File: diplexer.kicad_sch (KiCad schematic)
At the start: 5 parts, among them J22 BWSMA-KWE-Z001

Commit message: Start working on BOM, fix supply indoctors
Signed-off-by: Corey Minyard <corey@minyard.net>
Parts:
- L35: footprint Inductor_SMD:L_1206_3216Metric -> Inductor_SMD:L_0805_2012Metric_Pad1.05x1.20mm_HandSolder
- L44: footprint Inductor_SMD:L_1206_3216Metric -> Inductor_SMD:L_0603_1608Metric_Pad1.05x0.95mm_HandSolder
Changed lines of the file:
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@@
 			)
 		)
-		(property "Footprint" "Inductor_SMD:L_1206_3216Metric"
+		(property "Footprint" "Inductor_SMD:L_0603_1608Metric_Pad1.05x0.95mm_HandSolder"
 			(at 102.87 81.28 0)
 			(effects
@@
 			)
 		)
-		(property "Footprint" "Inductor_SMD:L_1206_3216Metric"
+		(property "Footprint" "Inductor_SMD:L_0805_2012Metric_Pad1.05x1.20mm_HandSolder"
 			(at 102.87 105.41 0)
 			(effects

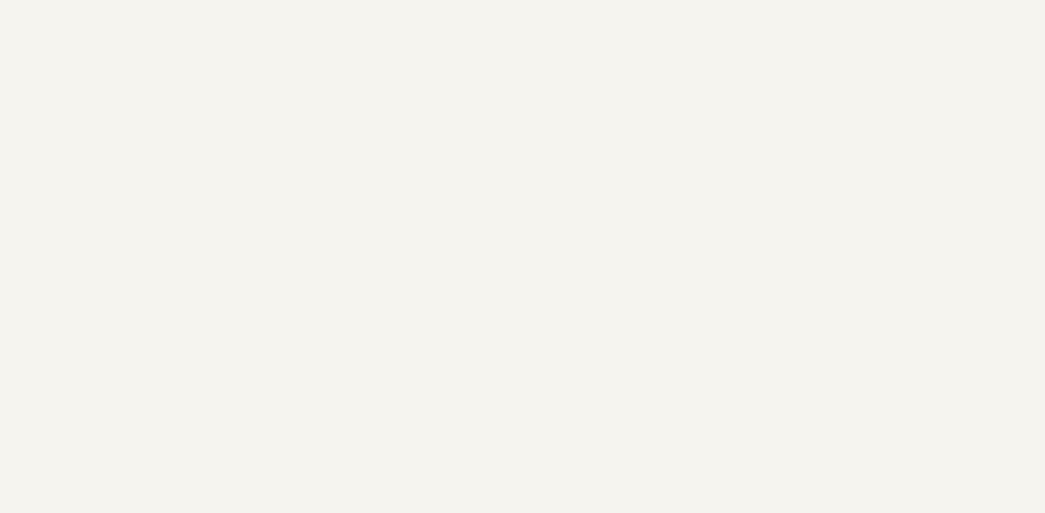
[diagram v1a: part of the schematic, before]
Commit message: Add fiduciaries and a control output
Signed-off-by: Corey Minyard <corey@minyard.net>
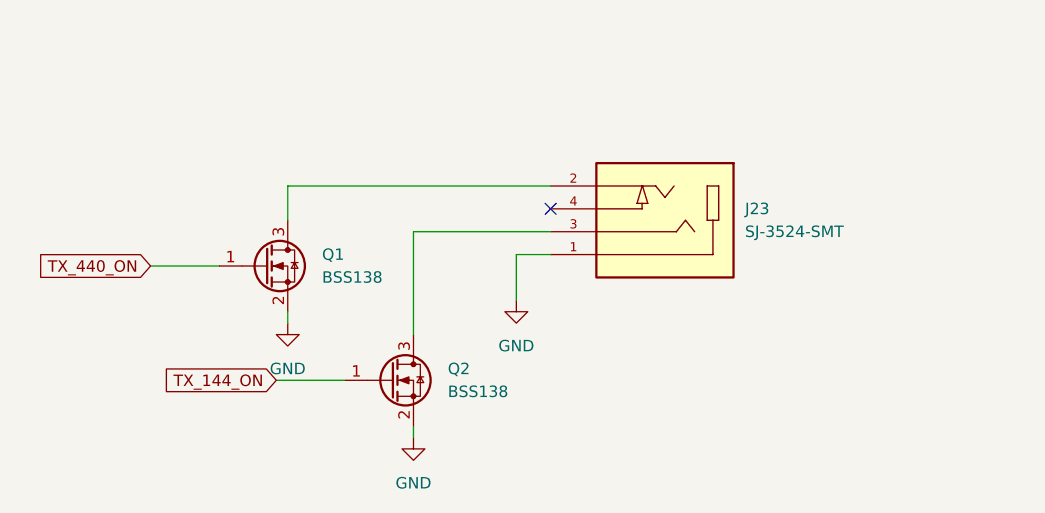
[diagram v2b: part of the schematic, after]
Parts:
- added J23: SJ-3524-SMT, footprints:CUI_SJ-3524-SMT, symbol Local Connectors:SJ-3524-SMT
- added Q1, Q2: BSS138, Package_TO_SOT_SMD:SOT-23, symbol Transistor_FET:BSS138
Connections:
- net GND: now also J23.1, Q1.2 (S), Q2.2 (S)
- new net: J23.2, Q1.3 (D)
- new net: J23.3, Q2.3 (D)
- new net TX_144_ON: Q2.1 (G)
- new net TX_440_ON: Q1.1 (G)
- no-connect marks 0 -> 1

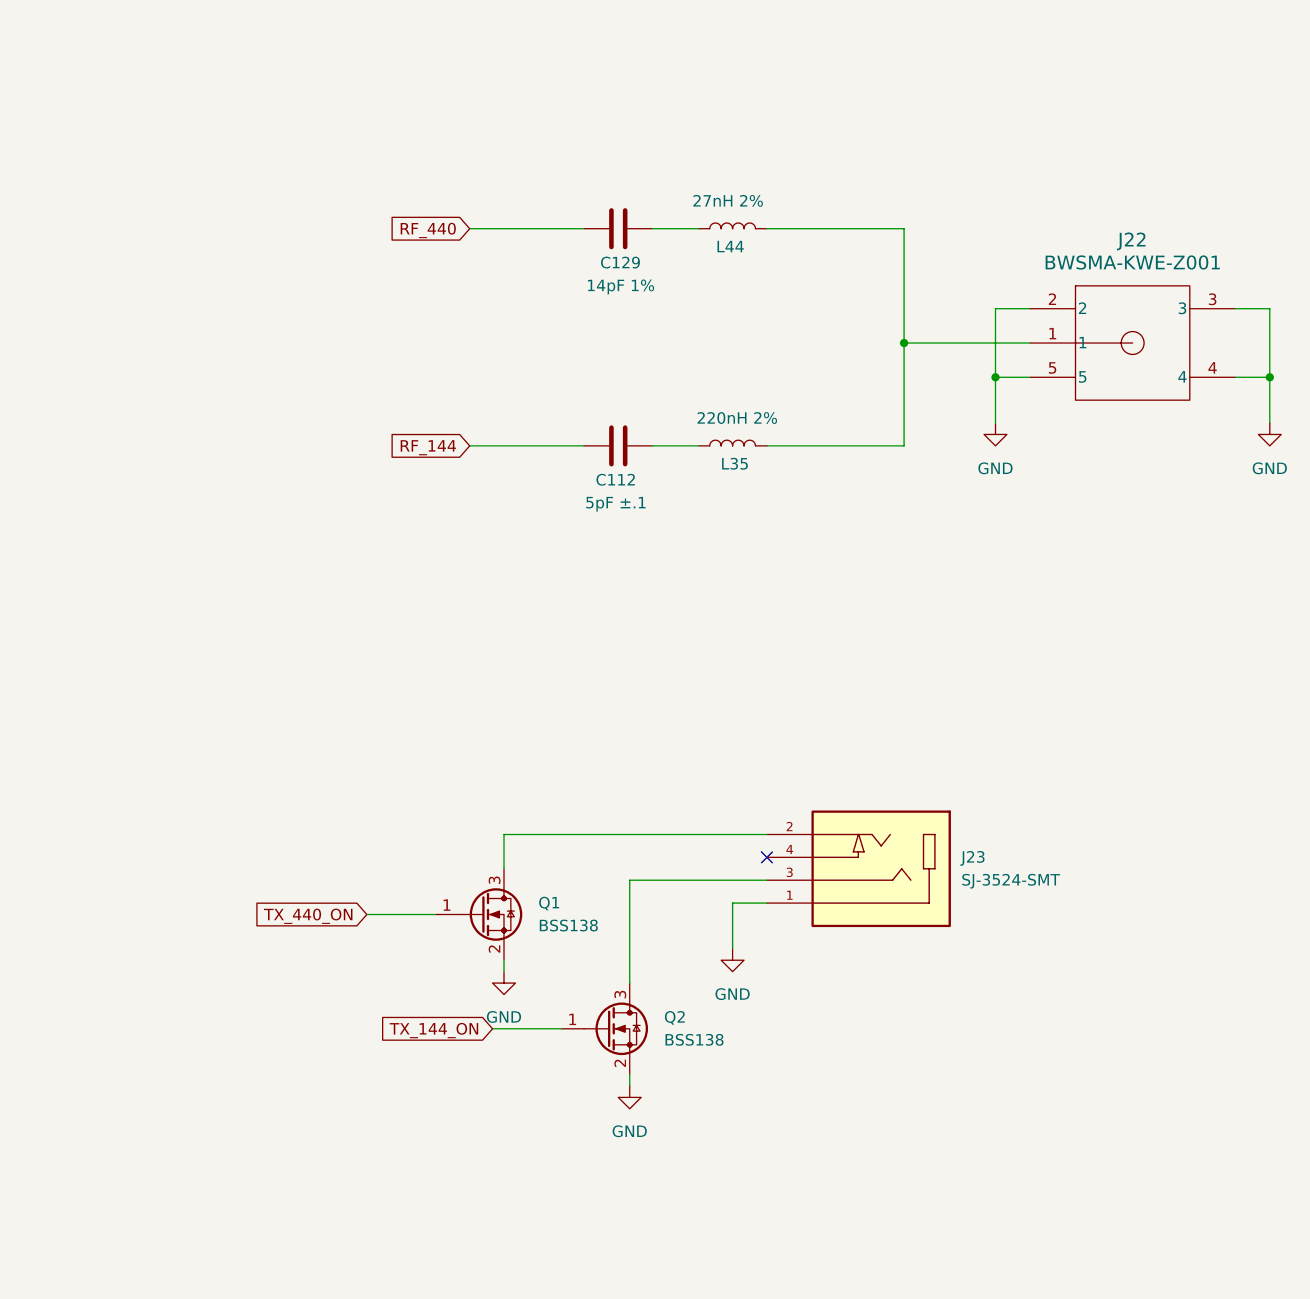
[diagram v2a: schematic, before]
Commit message: Add pull up on the PA enables
So they are off by default.

Signed-off-by: Corey Minyard <corey@minyard.net>
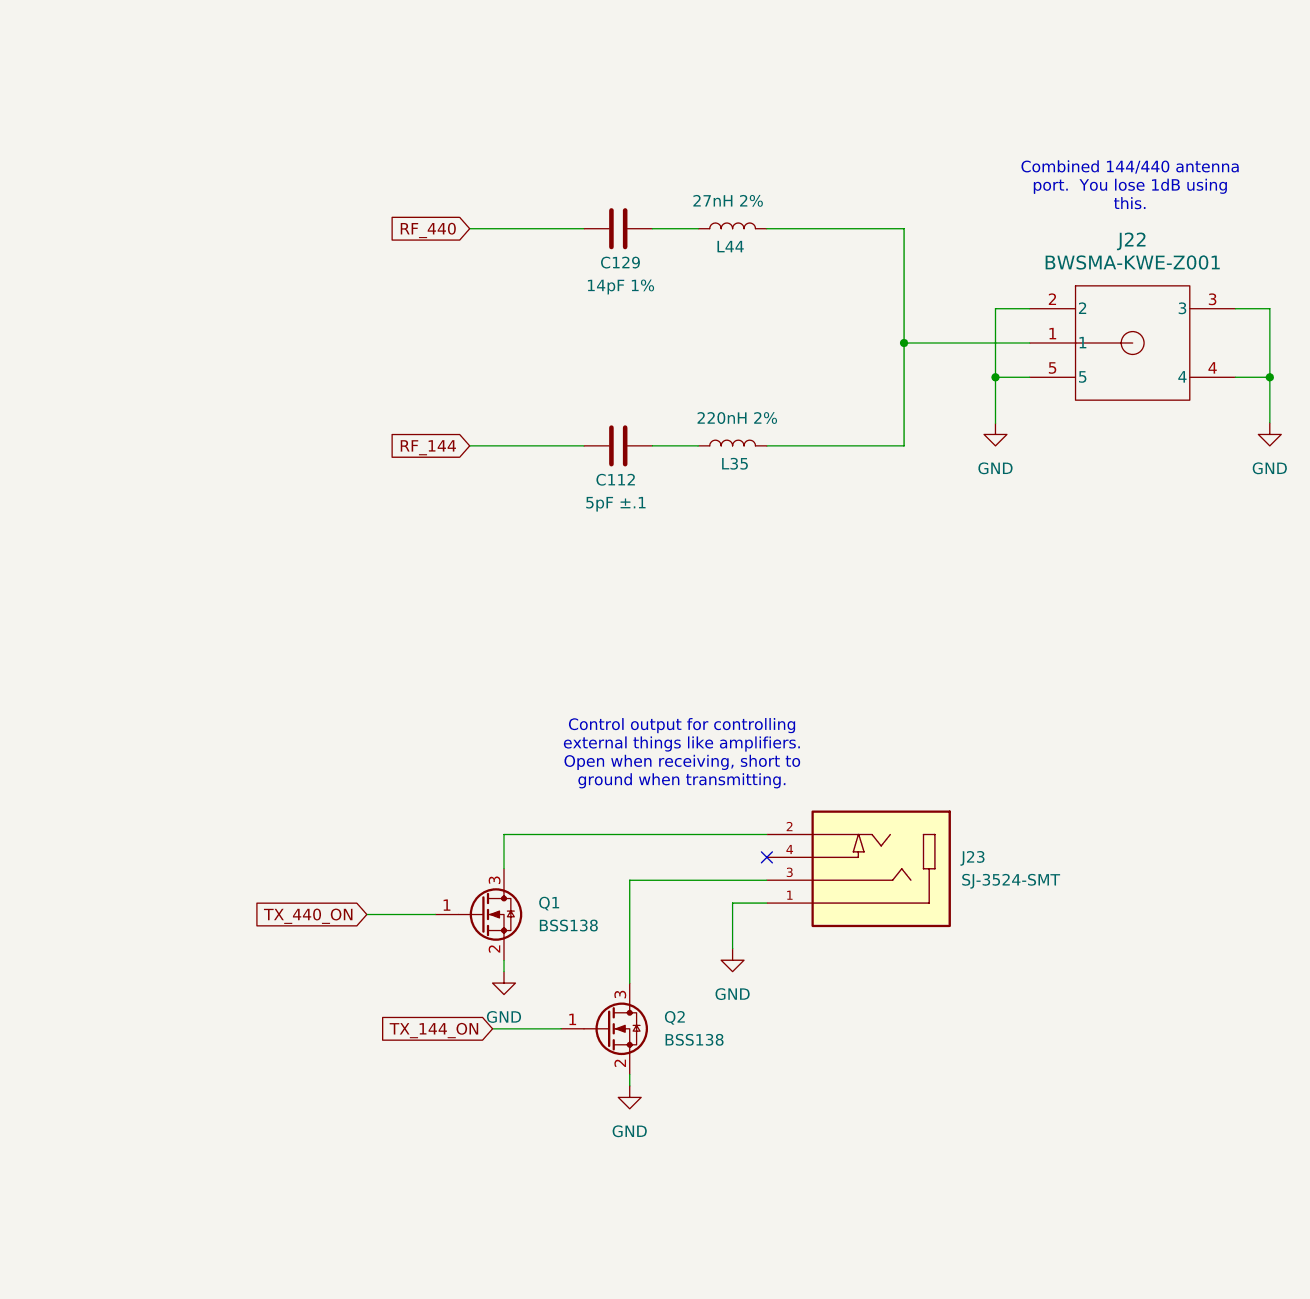
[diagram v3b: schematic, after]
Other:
- note added: "Combined 144/440 antenna port. You lose 1dB using this."
- note added: "Control output for controlling external things like amplifiers. Open when receiving, short to ground when transmitting."
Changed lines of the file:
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@@
 	(generator_version "9.0")
 	(paper "A4")
+	(text "Combined 144/440 antenna\nport.  You lose 1dB using\nthis."
+		(exclude_from_sim no)
+		(at 147.066 76.708 0)
+		(effects
+			(font
+				(size 1.27 1.27)
+			)
+		)
+	)
+	(text "Control output for controlling\nexternal things like amplifiers.\nOpen when receiving, short to\nground when transmitting."
+		(exclude_from_sim no)
+		(at 97.282 139.7 0)
+		(effects
+			(font
+				(size 1.27 1.27)
+			)
+		)
+	)
 	(junction
 		(at 121.92 93.98)

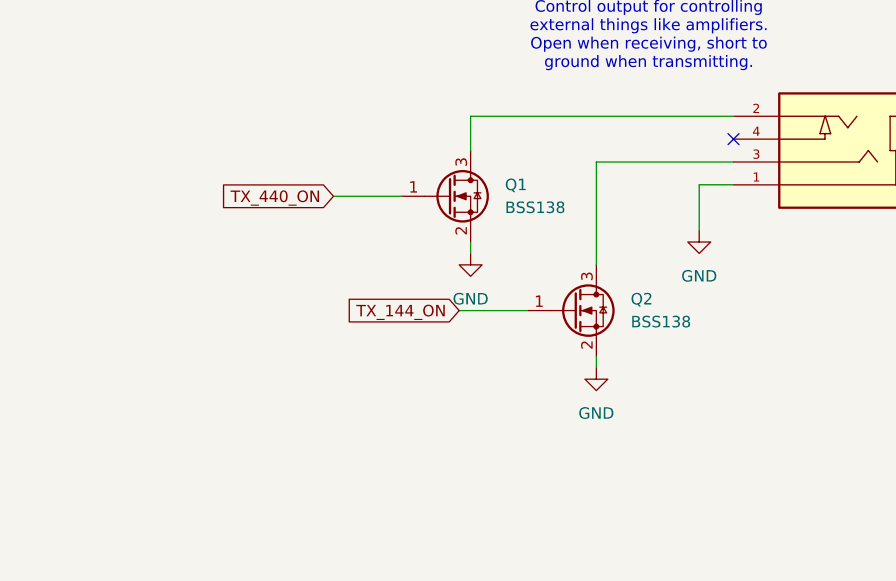
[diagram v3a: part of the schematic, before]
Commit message: Add pulldowns on the external control transistor inputs
So they are disabled by default.

Signed-off-by: Corey Minyard <corey@minyard.net>
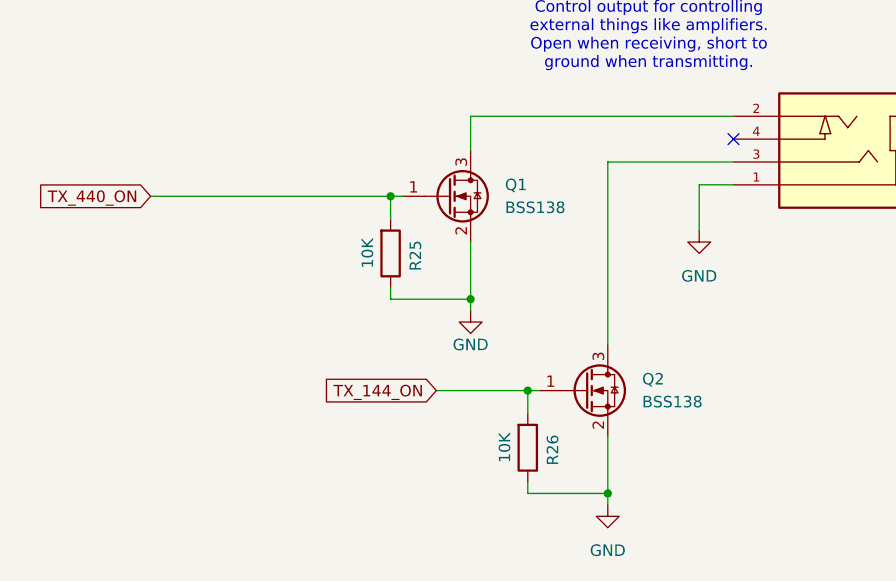
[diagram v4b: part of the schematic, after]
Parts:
- added R25, R26: 10K, Resistor_SMD:R_0402_1005Metric, symbol Device:R
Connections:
- net GND: now also R25.1, R26.1
- net TX_144_ON: now also R26.2
- net TX_440_ON: now also R25.2
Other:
- moved on the sheet: Q2

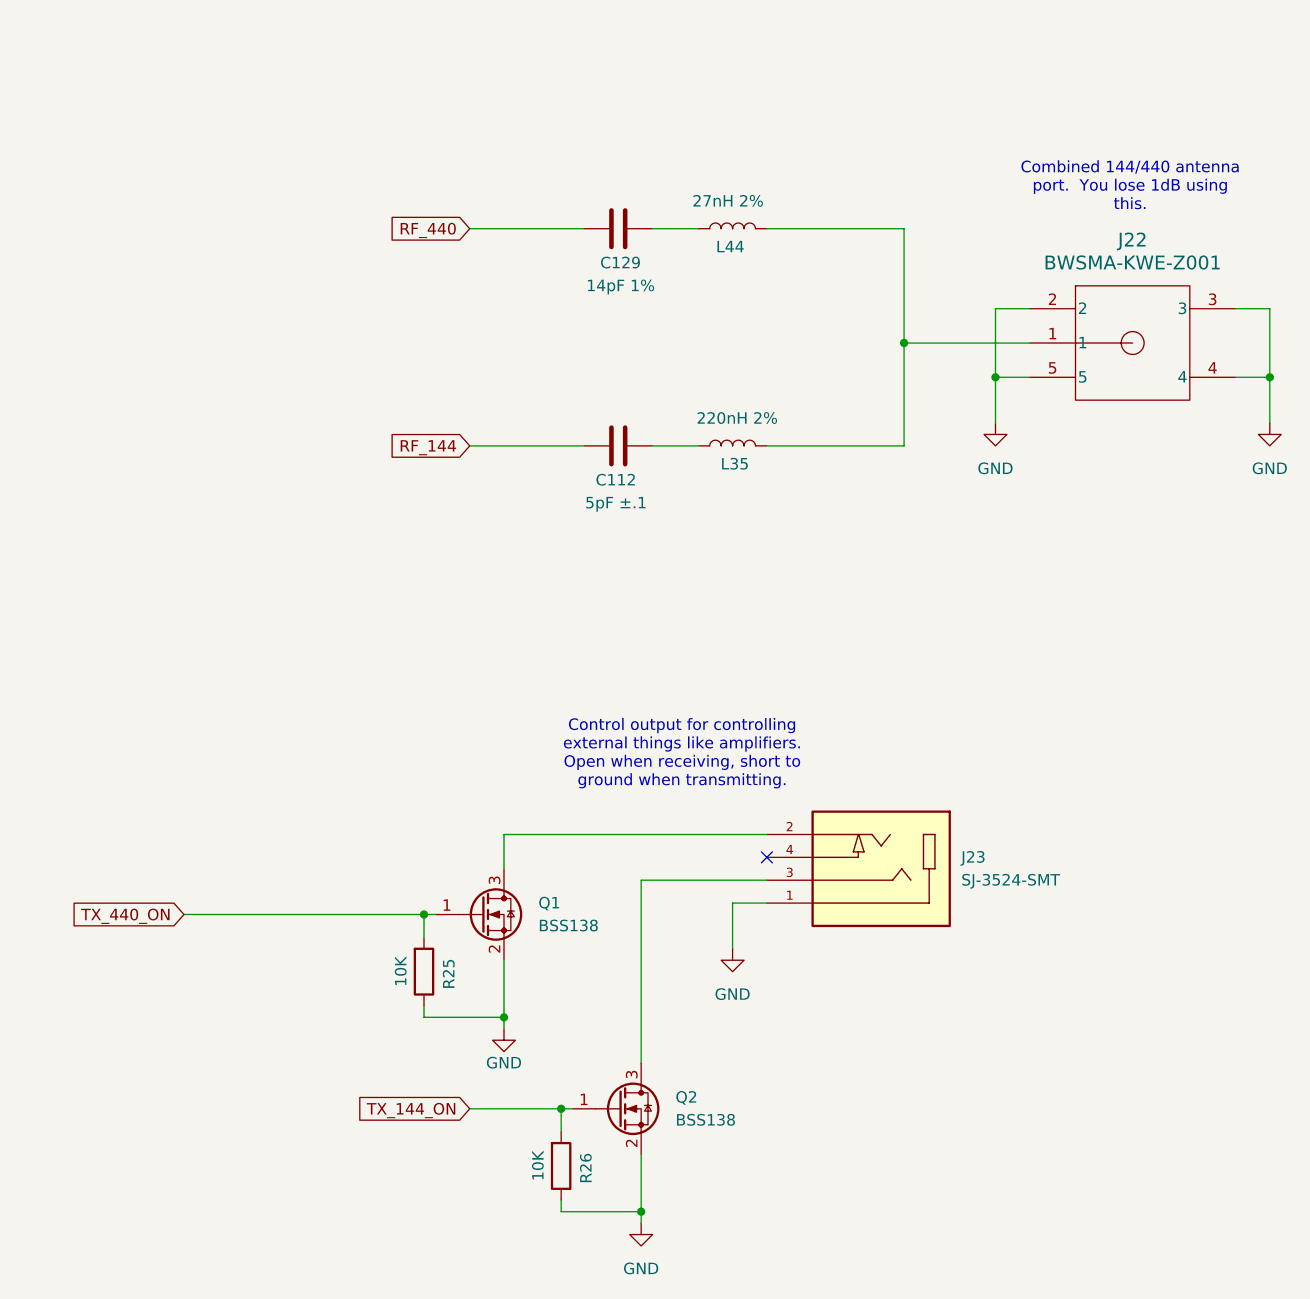
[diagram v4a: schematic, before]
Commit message: Add bleed-off inductor/resistors to the antenna jacks
Signed-off-by: Corey Minyard <corey@minyard.net>
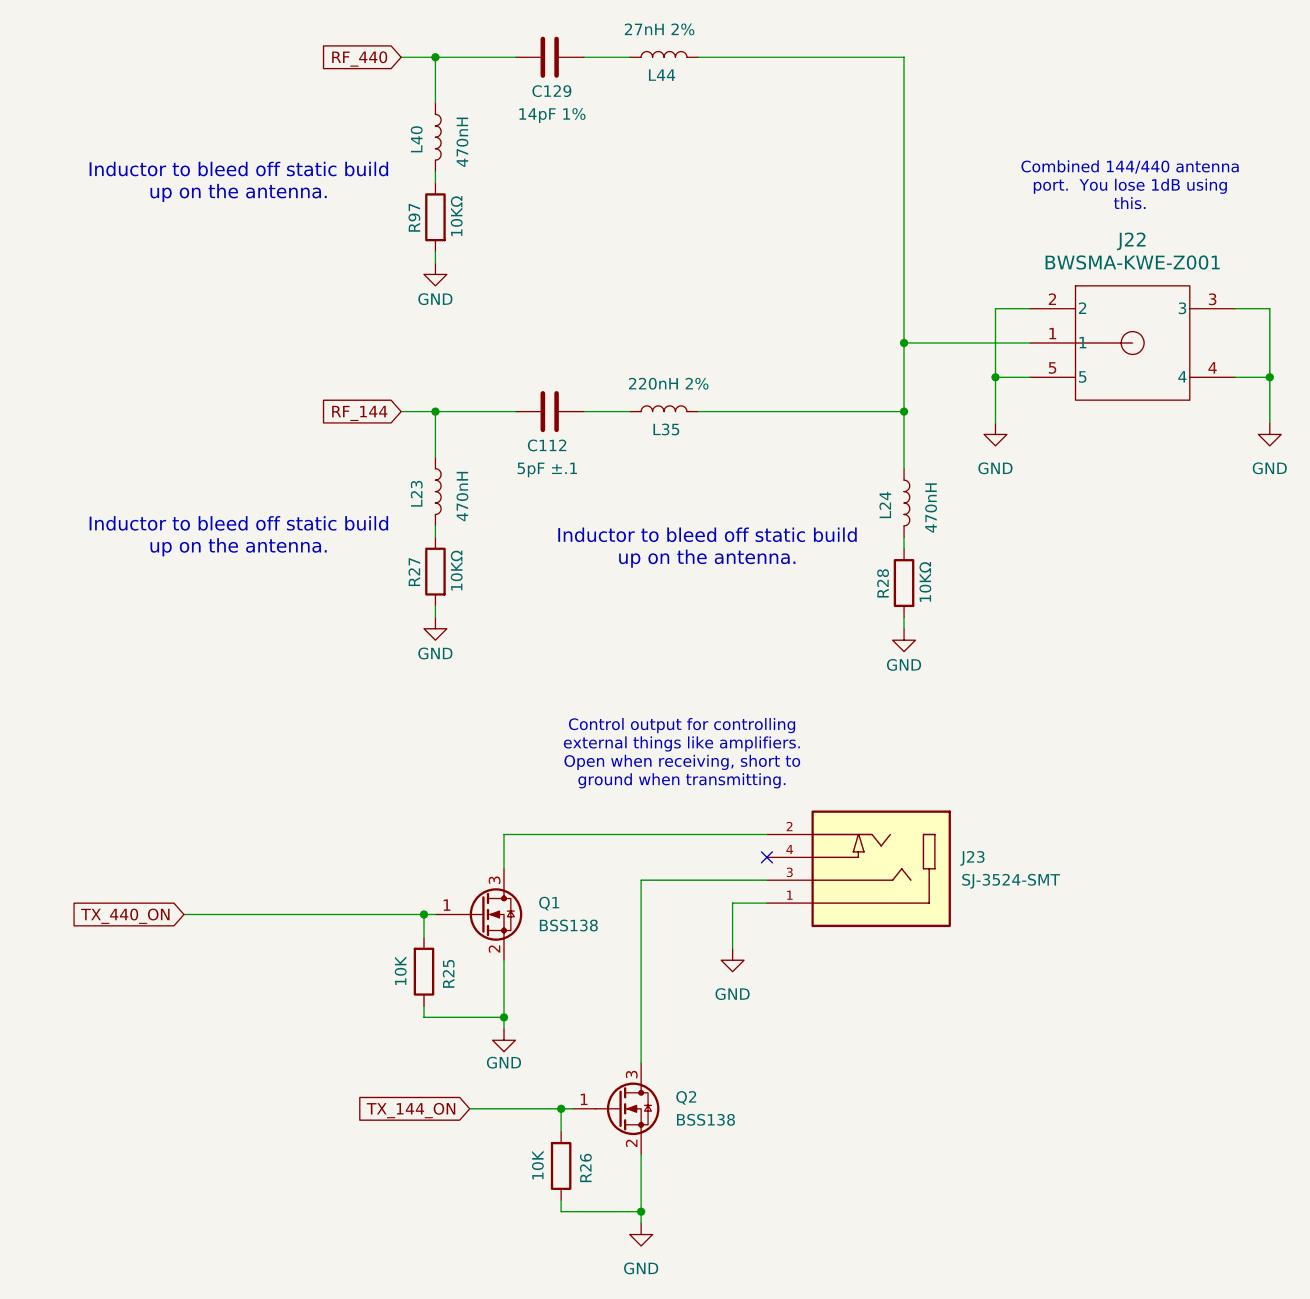
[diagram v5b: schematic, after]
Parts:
- added L23, L24, L40: 470nH, Inductor_SMD:L_0805_2012Metric_Pad1.05x1.20mm_HandSolder, symbol Device:L
- added R27, R28, R97: 10KΩ, Resistor_SMD:R_0402_1005Metric_Pad0.72x0.64mm_HandSolder, symbol Device:R
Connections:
- net GND: now also R27.2, R28.2, R97.2
- net RF_144: now also L23.1
- net RF_440: now also L40.1
- net at J22.1, L35.2, L44.1: now also L24.1
- new net: L24.2, R28.1
- new net: L23.2, R27.1
- new net: L40.2, R97.1
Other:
- note added: "Inductor to bleed off static build up on the antenna."
- moved on the sheet: C112, C129, L35, L44

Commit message: Add thermsistors by the PAs
Signed-off-by: Corey Minyard <corey@minyard.net>
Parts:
- R27, R28, R97: value 10KΩ -> 10K
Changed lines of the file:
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@@
 			)
 		)
-		(property "Value" "10KΩ"
+		(property "Value" "10K"
 			(at 124.333 122.936 90)
 			(effects
@@
 			)
 		)
-		(property "Value" "10KΩ"
+		(property "Value" "10K"
 			(at 72.263 82.296 90)
 			(effects
@@
 			)
 		)
-		(property "Value" "10KΩ"
+		(property "Value" "10K"
 			(at 72.263 121.666 90)
 			(effects
